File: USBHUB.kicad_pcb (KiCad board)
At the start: 4 copper layers, 214.6 x 214.6 mm, 214 parts, among them J1 USB_C_Receptacle, Q1 SI3421DV, Q2 SI3421DV, U1 CYPD3177_24x, U10 TPS20xxC, U11 USB_3_Type_A_Molex_484080003, U12 TPS20xxC, U13 USB_3_Type_A_Molex_484080003, U14 TPS20xxC, U15 USB_3_Type_A_Molex_484080003, U16 CYUSB3304-68LTXx, U2 TPS54331, U3 TLV75733PDBV, U4 TPS56637RPAR, U5 TVS2200DRVx, U6 PI3USB302-Ax, U7 TUSB522Px, U8 USB_3_Type_A_Molex_484080003, U9 TPS20xxC, Y1 26MHz

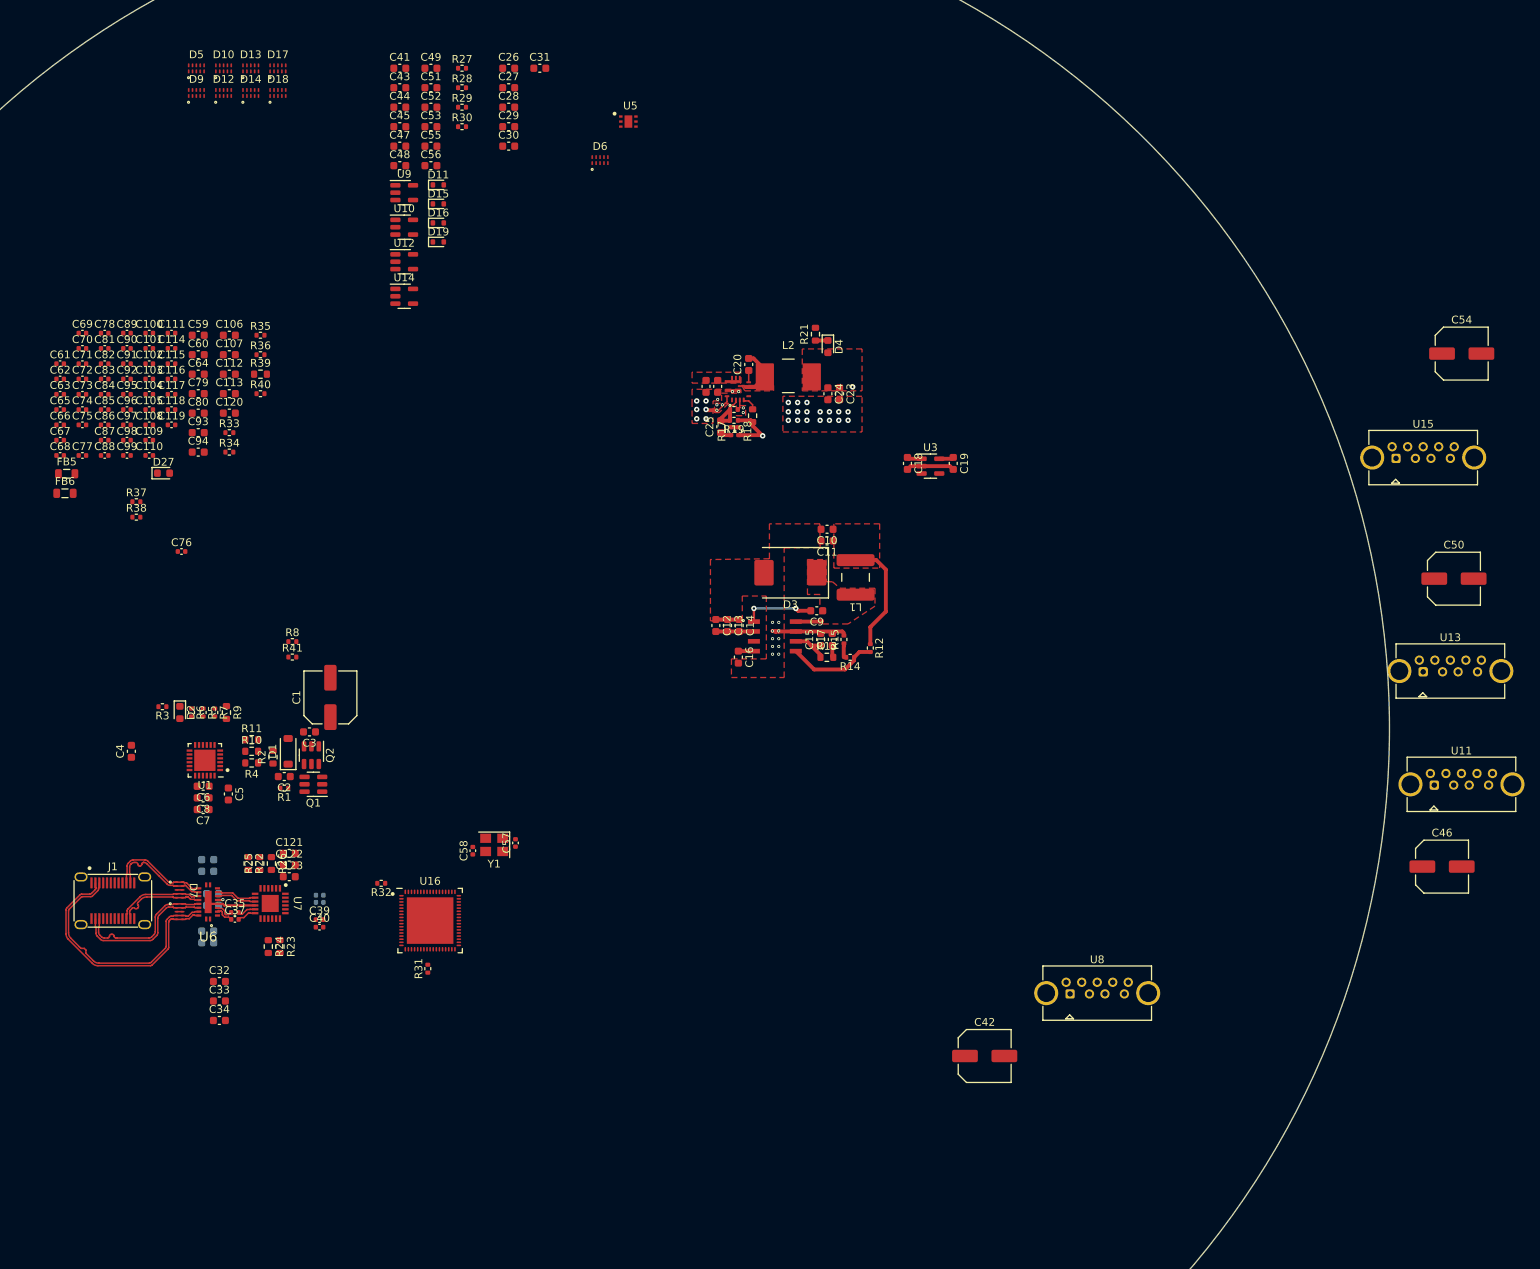
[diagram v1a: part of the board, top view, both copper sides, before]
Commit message: add RTL8153
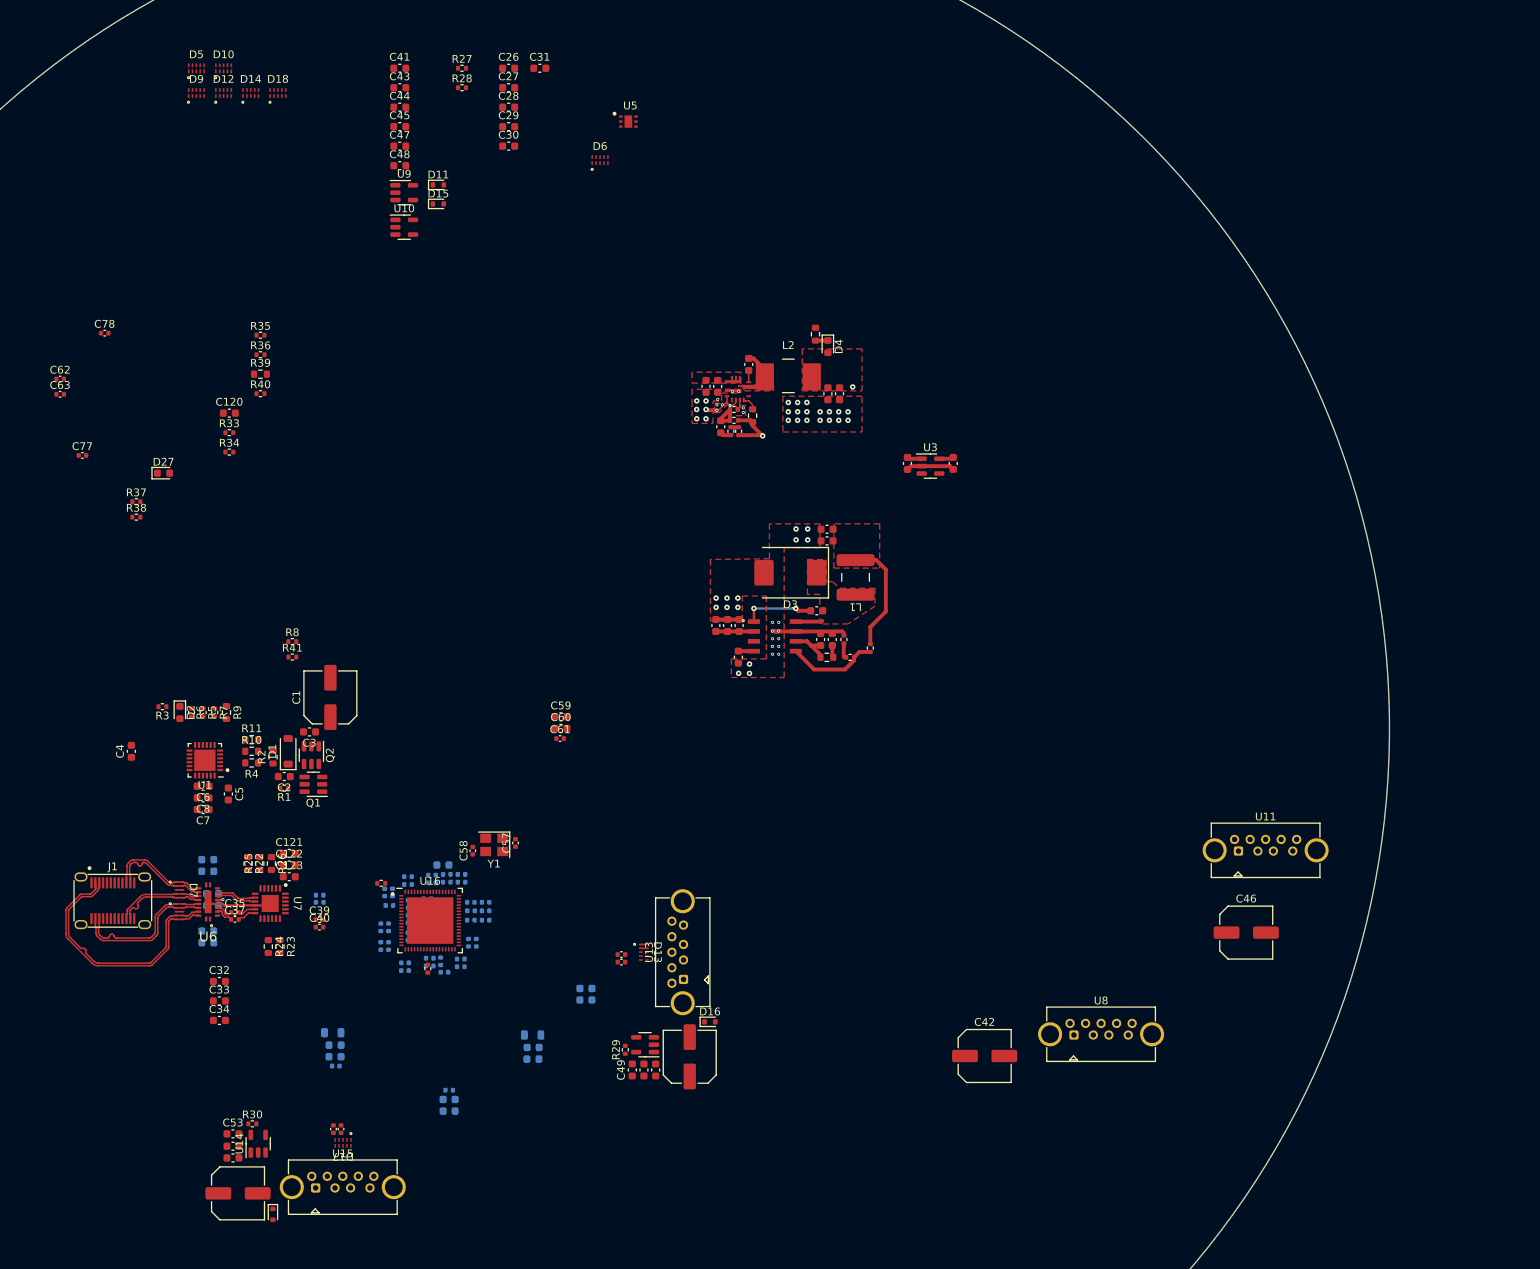
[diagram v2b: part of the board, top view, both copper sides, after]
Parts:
- C100, C101, C102, C103, C104, C105, C106, C107, C108, C109, C110, C111, C112, C113, C114, C115, C116, C117, C118, C119, C64, C65, C66, C67, C68, C69, C70, C71, C72, C73, C74, C75, C76, C79, C80, C81, C82, C83, C84, C85, C86, C87, C88, C93, C94, C95, C96, C97, C98, C99, FB5, FB6: moved to B.Cu
- moved C54 191.2 mm to (99.8, 175.7)
- moved U15 168.0 mm to (113.3, 174.9)
- moved D17 138.7 mm to (113.3, 169.2), turned to 180 degrees
- moved C53 132.3 mm to (99.2, 168.0)
- moved C49 131.6 mm to (150.6, 159.8), turned to 90 degrees
- moved C55 131.4 mm to (99.2, 169.6)
- moved R30 131.3 mm to (101.7, 166.7)
- moved C56 130.4 mm to (99.2, 171.1)
- moved C51 129.5 mm to (152.1, 159.8), turned to 90 degrees
- moved C52 127.4 mm to (153.6, 159.8), turned to 90 degrees
- moved D19 127.1 mm to (104.3, 178.4), turned to -90 degrees
- moved D13 124.6 mm to (152.1, 144.6), turned to -90 degrees
- moved R29 123.3 mm to (149.7, 157.2), turned to 90 degrees
- moved C50 116.1 mm to (158.0, 158.1), turned to 90 degrees
- moved U14 110.8 mm to (102.4, 169.3), turned to 90 degrees
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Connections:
- net HUB1_DS1_DM renamed HUB1_DS1_DN
- net HUB1_DS1_RXM renamed HUB1_DS1_RXN
- net HUB1_DS1_TXM renamed HUB1_DS1_TXN
- net HUB1_DS2_DM renamed HUB1_DS2_DN
- net HUB1_DS2_RXM renamed HUB1_DS2_RXN
- net HUB1_DS2_TXM renamed HUB1_DS2_TXN
- net HUB1_DS3_DM renamed HUB1_DS3_DN
- net HUB1_DS3_RXM renamed HUB1_DS3_RXN
- net HUB1_DS3_TXM renamed HUB1_DS3_TXN
- net HUB1_DS4_DM renamed HUB1_DS4_DN
- net HUB1_DS4_RXM renamed HUB1_DS4_RXN
- net HUB1_DS4_TXM renamed HUB1_DS4_TXN
- net Net-(U16-DS1_TXM) renamed /04 Hub Controller/HUB1_DS1_1_TXN
- net Net-(U16-DS1_TXP) renamed /04 Hub Controller/HUB1_DS1_1_TXP
- net Net-(U16-DS2_TXM) renamed /04 Hub Controller/HUB1_DS2_1_TXN
- net Net-(U16-DS2_TXP) renamed /04 Hub Controller/HUB1_DS2_1_TXP
- net Net-(U16-DS3_TXM) renamed /04 Hub Controller/HUB1_DS3_1_TXN
- net Net-(U16-DS3_TXP) renamed /04 Hub Controller/HUB1_DS3_1_TXP
- net Net-(U16-DS4_TXM) renamed /04 Hub Controller/HUB1_DS4_1_TXN
- net Net-(U16-DS4_TXP) renamed /04 Hub Controller/HUB1_DS4_1_TXP
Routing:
- net GND: track 31.7 -> 33.8 mm, vias 41 -> 54
- net HUB1_DS3_RXP: track 0.00 -> 0.78 mm
- net HUB1_DS3_RXN: track 0.00 -> 0.78 mm

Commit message: route power delivery controller
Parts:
- removed D18: PUSB3FR4Z, CakeUSB:PUSB3FR4Z
- removed D19: ESD5B5.0ST1G, Diode_SMD:D_SOD-523
- removed D27: RED, LED_SMD:LED_0603_1608Metric
- removed FB5, FB6: BLM21PG221SN1D, Inductor_SMD:L_0805_2012Metric
- removed U16: CYUSB3304-68LTXx, CakeUSB:CYUSB3304-68LTXx
- added C129: 100n, Capacitor_SMD:C_0402_1005Metric, F.Cu at (-59.6, 144.1)
- added C131: 4u7, Capacitor_SMD:C_0603_1608Metric, F.Cu at (-53.7, 125.5)
- added C132: 1u, Capacitor_SMD:C_0603_1608Metric, F.Cu at (-53.7, 128.0)
- added C133: 4u7, Capacitor_SMD:C_0603_1608Metric, F.Cu at (-53.7, 130.5)
- added C134: 4u7, Capacitor_SMD:C_0603_1608Metric, F.Cu at (-53.7, 133.0)
- added C135: 100n, Capacitor_SMD:C_0402_1005Metric, F.Cu at (-59.6, 146.1)
- added C136: 100n, Capacitor_SMD:C_0402_1005Metric, F.Cu at (-59.6, 148.0)
- added C137: 100n, Capacitor_SMD:C_0402_1005Metric, F.Cu at (-59.6, 150.0)
- added C138: 100n, Capacitor_SMD:C_0402_1005Metric, F.Cu at (-59.6, 152.0)
- added C139: 100n, Capacitor_SMD:C_0402_1005Metric, F.Cu at (-59.6, 153.9)
- added C140: 100n, Capacitor_SMD:C_0402_1005Metric, F.Cu at (-59.6, 155.9)
- added C141: 100n, Capacitor_SMD:C_0402_1005Metric, F.Cu at (-56.7, 144.1)
- added C142: 100n, Capacitor_SMD:C_0402_1005Metric, F.Cu at (-56.7, 146.1)
- added C143: 100n, Capacitor_SMD:C_0402_1005Metric, F.Cu at (-56.7, 148.0)
- added C144: 100n, Capacitor_SMD:C_0402_1005Metric, F.Cu at (-56.7, 150.0)
- added C145: 100n, Capacitor_SMD:C_0402_1005Metric, F.Cu at (-56.7, 152.0)
- added C146: 100n, Capacitor_SMD:C_0402_1005Metric, F.Cu at (-56.7, 153.9)
- added C147: 10n, Capacitor_SMD:C_0402_1005Metric, F.Cu at (-56.7, 155.6)
- added C148: 10n, Capacitor_SMD:C_0402_1005Metric, F.Cu at (-53.9, 144.1)
- added C149: 10n, Capacitor_SMD:C_0402_1005Metric, F.Cu at (-53.9, 146.1)
- added C150: 1n/2KV, Capacitor_SMD:C_0402_1005Metric, F.Cu at (83.6, 266.0)
- added C151: 10n, Capacitor_SMD:C_0402_1005Metric, F.Cu at (-53.9, 148.0)
- added C152: 10n, Capacitor_SMD:C_0402_1005Metric, F.Cu at (-53.9, 150.0)
- added FB1: BLM21PG221SN1D, Inductor_SMD:L_0805_2012Metric, F.Cu at (-60.2, 187.3)
- added FB2: BLM21PG221SN1D, Inductor_SMD:L_0805_2012Metric, F.Cu at (-60.2, 190.1)
- added J2: R-RJ45R08P-C000, CakeUSB:R-RJ45R08P-C000, F.Cu at (-72.5, 133.9)
- added R42: 2k49_1%, Resistor_SMD:R_0603_1608Metric, F.Cu at (-53.7, 135.6)
- added R43: 10k, Resistor_SMD:R_0402_1005Metric, F.Cu at (-51.0, 147.8)
- added R44: 75, Resistor_SMD:R_0603_1608Metric, F.Cu at (-53.7, 138.1)
- added R45: 75, Resistor_SMD:R_0603_1608Metric, F.Cu at (-49.7, 125.5)
- added R46: 75, Resistor_SMD:R_0603_1608Metric, F.Cu at (-49.7, 128.0)
- added R47: 75, Resistor_SMD:R_0603_1608Metric, F.Cu at (-49.7, 130.5)
- added R48: 1k, Resistor_SMD:R_0603_1608Metric, F.Cu at (-49.7, 133.0)
- added R49: 1k, Resistor_SMD:R_0603_1608Metric, F.Cu at (-49.7, 135.6)
- added T1: G24P02S, CakeUSB:G24P02S, F.Cu at (-72.5, 149.7)
- added Y2: 25MHz 18pF, Crystal:Crystal_SMD_2016-4Pin_2.0x1.6mm, F.Cu at (-50.5, 144.9)
- C100, C73: value 10n -> 1u; footprint Capacitor_SMD:C_0402_1005Metric -> Capacitor_SMD:C_0603_1608Metric; moved to F.Cu
- C101, C103, C70, C74, C76: value 1n -> 100n; moved to F.Cu
- C102, C104, C75, C83, C85: moved to F.Cu
- C105, C72, C99: value 1n -> 22u; footprint Capacitor_SMD:C_0402_1005Metric -> Capacitor_SMD:C_0603_1608Metric; moved to F.Cu
- C106: value 22u -> 1u; moved to F.Cu
- C107, C80: value 1u -> 100n; footprint Capacitor_SMD:C_0603_1608Metric -> Capacitor_SMD:C_0402_1005Metric; moved to F.Cu
- C108, C110, C66, C81, C95: value 100n -> 10n; moved to F.Cu
- C109, C111, C71, C82, C84, C88: value 10n -> 100n; moved to F.Cu
- C112, C79, C93: value 22u -> 10n; footprint Capacitor_SMD:C_0603_1608Metric -> Capacitor_SMD:C_0402_1005Metric; moved to F.Cu
- C113: value 1u -> 22u; moved to F.Cu
- C114, C116, C118, C36: footprint Capacitor_SMD:C_0402_1005Metric -> Capacitor_SMD:C_0603_1608Metric; moved to F.Cu
- C115, C119: value 10n -> 150u; footprint Capacitor_SMD:C_0402_1005Metric -> Capacitor_SMD:C_Elec_6.3x7.7; moved to F.Cu
- C117: value 10n -> 100n; footprint Capacitor_SMD:C_0402_1005Metric -> Capacitor_SMD:C_0603_1608Metric; moved to F.Cu
- C120: value 22u -> 100n
- C121, C124: value 10u -> 100n
- C123: value 100n -> 150u; footprint Capacitor_SMD:C_0603_1608Metric -> Capacitor_SMD:C_Elec_6.3x7.7
- C126: value 100n -> 27p; footprint Capacitor_SMD:C_0603_1608Metric -> Capacitor_SMD:C_0402_1005Metric; moved to F.Cu
- C127: value 10u -> 27p; footprint Capacitor_SMD:C_0603_1608Metric -> Capacitor_SMD:C_0402_1005Metric; moved to F.Cu
- C128: value 100n -> 10u
- C130: value 10u -> 1u
- C26, C27, C28, C29, C44, C45, C47, C48, C49, C55, C56: footprint Capacitor_SMD:C_0603_1608Metric -> Capacitor_SMD:C_0402_1005Metric
- C35, C38: value 100n -> 10u; footprint Capacitor_SMD:C_0402_1005Metric -> Capacitor_SMD:C_0603_1608Metric
- C37: footprint Capacitor_SMD:C_0402_1005Metric -> Capacitor_SMD:C_0603_1608Metric
- C39, C40: value 100n -> 10u; footprint Capacitor_SMD:C_0402_1005Metric -> Capacitor_SMD:C_0603_1608Metric; moved to B.Cu
- C41, C43, D7: moved to B.Cu
- C42: value 150u -> 100n; footprint Capacitor_SMD:C_Elec_6.3x7.7 -> Capacitor_SMD:C_0603_1608Metric; moved to B.Cu
- C46, C54: value 150u -> 100n; footprint Capacitor_SMD:C_Elec_6.3x7.7 -> Capacitor_SMD:C_0402_1005Metric
- C50: value 150u -> 10p; footprint Capacitor_SMD:C_Elec_6.3x7.7 -> Capacitor_SMD:C_0402_1005Metric
- C51: value 100n -> 10p; footprint Capacitor_SMD:C_0603_1608Metric -> Capacitor_SMD:C_0402_1005Metric
- C52: value 100n -> 22u
- C53: value 100n -> 1u
- C57: value 10p -> 1u; footprint Capacitor_SMD:C_0402_1005Metric -> Capacitor_SMD:C_0603_1608Metric
- C58: value 10p -> 10n
- C59: value 22u -> 100n; footprint Capacitor_SMD:C_0603_1608Metric -> Capacitor_SMD:C_0402_1005Metric
- C60: value 1u -> 10n; footprint Capacitor_SMD:C_0603_1608Metric -> Capacitor_SMD:C_0402_1005Metric
- C61, C63, C90, C92: value 100n -> 1n
- C62, C77, C89, C91: value 100n -> 10n
- C64: value 1u -> 10n; footprint Capacitor_SMD:C_0603_1608Metric -> Capacitor_SMD:C_0402_1005Metric; moved to F.Cu
- C65, C67, C69, C96, C98: value 10n -> 1n; moved to F.Cu
- C68, C97: value 1n -> 10n; moved to F.Cu
- C86: value 10n -> 22u; footprint Capacitor_SMD:C_0402_1005Metric -> Capacitor_SMD:C_0603_1608Metric; moved to F.Cu
- C87: value 100n -> 1u; footprint Capacitor_SMD:C_0402_1005Metric -> Capacitor_SMD:C_0603_1608Metric; moved to F.Cu
- C94: value 1u -> 1n; footprint Capacitor_SMD:C_0603_1608Metric -> Capacitor_SMD:C_0402_1005Metric; moved to F.Cu
- D11: value ESD5B5.0ST1G -> PUSB3FR4Z; footprint Diode_SMD:D_SOD-523 -> CakeUSB:PUSB3FR4Z
- D14: value PUSB3FR4Z -> RED; footprint CakeUSB:PUSB3FR4Z -> LED_SMD:LED_0603_1608Metric
- D17: value PUSB3FR4Z -> ESD5B5.0ST1G; footprint CakeUSB:PUSB3FR4Z -> Diode_SMD:D_SOD-523
- R1: footprint Resistor_SMD:R_0402_1005Metric -> Resistor_SMD:R_0603_1608Metric
- R12: value 10k -> 5k1; footprint Resistor_SMD:R_0402_1005Metric -> Resistor_SMD:R_0603_1608Metric
- R13: value 953 -> 10k; footprint Resistor_SMD:R_0603_1608Metric -> Resistor_SMD:R_0402_1005Metric
- R14: value 10k -> 953; footprint Resistor_SMD:R_0402_1005Metric -> Resistor_SMD:R_0603_1608Metric
- R16: value 100k -> 10k; footprint Resistor_SMD:R_0603_1608Metric -> Resistor_SMD:R_0402_1005Metric
- R17: value 10k -> 100k; footprint Resistor_SMD:R_0402_1005Metric -> Resistor_SMD:R_0603_1608Metric
- R19: value 73k2 -> 10k
- R20: value 10k -> 73k2
- R21, R39: value 5k1 -> 10k; footprint Resistor_SMD:R_0603_1608Metric -> Resistor_SMD:R_0402_1005Metric
- R23: value 1k -> 5k1
- R27: value 10k -> 1k; footprint Resistor_SMD:R_0402_1005Metric -> Resistor_SMD:R_0603_1608Metric
- R28: value 10k -> 200_1%
- R29: value 10k -> 6k04_1%
- R31: value 200_1% -> 10k
- R32: value 6k04_1% -> 10k
- R35, R36: value 10k -> 2k
- R37: value 2k -> 5k1; footprint Resistor_SMD:R_0402_1005Metric -> Resistor_SMD:R_0603_1608Metric
- R38, R41: value 2k -> 10k
- R9: value 5k1 -> 2k; footprint Resistor_SMD:R_0603_1608Metric -> Resistor_SMD:R_0402_1005Metric
- U10, U9: value TPS20xxC -> USB_3_Type_A_Molex_484080003; footprint Package_TO_SOT_SMD:SOT-23-5 -> CakeUSB:Molex_484080003
- U11: value USB_3_Type_A_Molex_484080003 -> CYUSB3304-68LTXx; footprint CakeUSB:Molex_484080003 -> CakeUSB:CYUSB3304-68LTXx
- U13: value USB_3_Type_A_Molex_484080003 -> TPS20xxC; footprint CakeUSB:Molex_484080003 -> Package_TO_SOT_SMD:SOT-23-5
- U15: value USB_3_Type_A_Molex_484080003 -> RTL8153-VB-CG; footprint CakeUSB:Molex_484080003 -> CakeUSB:RTL8153B-VB-CG
- moved C31 317.3 mm to (-91.8, 248.8)
- moved C30 305.8 mm to (-91.8, 246.3)
- moved C47 284.3 mm to (-80.3, 241.9)
- moved C44 283.7 mm to (-80.3, 235.9)
- moved C45 283.3 mm to (-80.3, 237.9)
- moved D11 275.1 mm to (-70.9, 238.3)
- moved D15 273.9 mm to (-82.0, 226.8)
- moved D12 267.5 mm to (-70.9, 241.4)
- moved R28 266.0 mm to (-67.2, 213.3)
- moved D10 265.1 mm to (-70.9, 235.1)
- moved U9 261.5 mm to (-60.6, 234.7)
- moved D9 258.0 mm to (-70.9, 231.9)
- moved D14 254.3 mm to (-63.7, 227.3)
- moved D16 254.2 mm to (-82.0, 229.3)
- moved U13 249.7 mm to (-81.3, 218.9), turned to 0 degrees
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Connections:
- C100 pad 1: +1V2 -> Net-(C100-Pad1)
- C101 pad 1: +1V2 -> Net-(C100-Pad1)
- C102 pad 1: +1V2 -> Net-(C100-Pad1)
- C103 pad 1: +1V2 -> +3V3
- C104 pad 1: +1V2 -> +3V3
- C105 pad 1: +1V2 -> +3V3
- C106 pad 1: Net-(C106-Pad1) -> +3V3
- C107 pad 1: Net-(C106-Pad1) -> +3V3
- C108 pad 1: Net-(C106-Pad1) -> +3V3
- C109 pad 1: Net-(C106-Pad1) -> +3V3
- C113 pad 1: +3V3 -> /04 Hub Controller/RESETN
- C114 pad 1: +3V3 -> GND
- C114 pad 2: GND -> +5V
- C115 pad 1: +3V3 -> GND
- C115 pad 2: GND -> /03 USB_DFP/USB_DS1_VBUS
- C116 pad 1: +3V3 -> GND
- C116 pad 2: GND -> /03 USB_DFP/USB_DS1_VBUS
- C117 pad 1: +3V3 -> GND
- C117 pad 2: GND -> /03 USB_DFP/USB_DS1_VBUS
- C118 pad 1: +3V3 -> GND
- C118 pad 2: GND -> +5V
- C119 pad 1: +3V3 -> GND
- C119 pad 2: GND -> /03 USB_DFP/USB_DS2_VBUS
- C120 pad 1: /04 Hub Controller/RESETN -> GND
- C120 pad 2: GND -> /03 USB_DFP/USB_DS2_VBUS
- C121 pad 1: +3V3 -> GND
- C121 pad 2: GND -> /03 USB_DFP/USB_DS2_VBUS
- C122 pad 1: +3V3 -> GND
- C122 pad 2: GND -> +5V
- C123 pad 1: +3V3 -> GND
- C123 pad 2: GND -> /03 USB_DFP/USB_DS3_VBUS
- C124 pad 1: +3V3 -> GND
- C124 pad 2: GND -> /03 USB_DFP/USB_DS3_VBUS
- C125 pad 1: +3V3 -> GND
- C125 pad 2: GND -> /03 USB_DFP/USB_DS3_VBUS
- C126 pad 1: +3V3 -> Net-(U15A-CKXTAL1)
- C127 pad 1: +3V3 -> Net-(U15A-CKXTAL2)
- C128 pad 1: +3V3 -> GND
- C128 pad 2: GND -> +5V
- C130 pad 1: +3V3 -> Net-(U15B-DVDD10_UPS_REGOUT)
- C35 pad 1: /02 USB UFP/UFP_TX- -> +3V3
- C35 pad 2: /02 USB UFP/UFP_TX_A_N -> GND
- C36 pad 1: /02 USB UFP/UFP_RX_B_N -> +3V3
- C36 pad 2: USB_UFP_RXN -> GND
- C37 pad 1: /02 USB UFP/UFP_TX+ -> +3V3
- C37 pad 2: /02 USB UFP/UFP_TX_A_P -> GND
- C38 pad 1: /02 USB UFP/UFP_RX_B_P -> +3V3
- C38 pad 2: USB_UFP_RXP -> GND
- C39 pad 1: /02 USB UFP/UFP_TX_B_N -> +3V3
- C39 pad 2: USB_UFP_TXN -> GND
- C40 pad 1: /02 USB UFP/UFP_TX_B_P -> +3V3
- C40 pad 2: USB_UFP_TXP -> GND
- C41 pad 1: GND -> +3V3
- C41 pad 2: +5V -> GND
- C42 pad 1: GND -> +3V3
- C42 pad 2: /03 USB_DFP/USB_DS1_VBUS -> GND
- C43 pad 1: GND -> +3V3
- C43 pad 2: /03 USB_DFP/USB_DS1_VBUS -> GND
- C44 pad 1: GND -> /02 USB UFP/UFP_RX_B_N
- C44 pad 2: /03 USB_DFP/USB_DS1_VBUS -> USB_UFP_RXN
- C45 pad 1: GND -> /02 USB UFP/UFP_RX_B_P
- C45 pad 2: +5V -> USB_UFP_RXP
- C46 pad 1: GND -> /02 USB UFP/UFP_TX-
- C46 pad 2: /03 USB_DFP/USB_DS2_VBUS -> /02 USB UFP/UFP_TX_A_N
- C47 pad 1: GND -> /02 USB UFP/UFP_TX_B_N
- C47 pad 2: /03 USB_DFP/USB_DS2_VBUS -> USB_UFP_TXN
- C48 pad 1: GND -> /02 USB UFP/UFP_TX+
- C48 pad 2: /03 USB_DFP/USB_DS2_VBUS -> /02 USB UFP/UFP_TX_A_P
- C49 pad 1: GND -> /02 USB UFP/UFP_TX_B_P
- C49 pad 2: +5V -> USB_UFP_TXP
- C50 pad 1: GND -> Net-(U11-XTL_OUT)
- C50 pad 2: /03 USB_DFP/USB_DS3_VBUS -> GND
- C51 pad 1: GND -> Net-(U11-XTL_IN)
- C51 pad 2: /03 USB_DFP/USB_DS3_VBUS -> GND
- C52 pad 1: GND -> +1V2
- C52 pad 2: /03 USB_DFP/USB_DS3_VBUS -> GND
- C53 pad 1: GND -> +1V2
- C53 pad 2: +5V -> GND
- C54 pad 1: GND -> +1V2
- C54 pad 2: /03 USB_DFP/USB_DS4_VBUS -> GND
- C55 pad 1: GND -> /04 Hub Controller/HUB1_DS1_1_TXP
- C55 pad 2: /03 USB_DFP/USB_DS4_VBUS -> HUB1_DS1_TXP
- C56 pad 1: GND -> /04 Hub Controller/HUB1_DS1_1_TXN
- C56 pad 2: /03 USB_DFP/USB_DS4_VBUS -> HUB1_DS1_TXN
- C57 pad 1: Net-(U16-XTL_OUT) -> +1V2
- C58 pad 1: Net-(U16-XTL_IN) -> +1V2
- C62 pad 1: /04 Hub Controller/HUB1_DS1_1_TXP -> +1V2
- C62 pad 2: HUB1_DS1_TXP -> GND
- C63 pad 1: /04 Hub Controller/HUB1_DS1_1_TXN -> +1V2
- C63 pad 2: HUB1_DS1_TXN -> GND
- C70 pad 1: +1V2 -> /04 Hub Controller/HUB1_DS2_1_TXP
- C70 pad 2: GND -> HUB1_DS2_TXP
- C71 pad 1: +1V2 -> /04 Hub Controller/HUB1_DS2_1_TXN
- C71 pad 2: GND -> HUB1_DS2_TXN
- C72 pad 1: +1V2 -> /04 Hub Controller/DVDD12
- C73 pad 1: +1V2 -> /04 Hub Controller/DVDD12
- C74 pad 1: +1V2 -> /04 Hub Controller/DVDD12
- C75 pad 1: +1V2 -> /04 Hub Controller/DVDD12
- C76 pad 1: +1V2 -> /04 Hub Controller/DVDD12
- C77 pad 1: /04 Hub Controller/HUB1_DS2_1_TXP -> /04 Hub Controller/DVDD12
- C77 pad 2: HUB1_DS2_TXP -> GND
- C78 pad 1: /04 Hub Controller/HUB1_DS2_1_TXN -> /04 Hub Controller/DVDD12
- C78 pad 2: HUB1_DS2_TXN -> GND
- C82 pad 1: /04 Hub Controller/DVDD12 -> /04 Hub Controller/HUB1_DS3_1_TXP
- C82 pad 2: GND -> HUB1_DS3_TXP
- C83 pad 1: /04 Hub Controller/DVDD12 -> /04 Hub Controller/HUB1_DS3_1_TXN
- C83 pad 2: GND -> HUB1_DS3_TXN
- C84 pad 1: /04 Hub Controller/DVDD12 -> /04 Hub Controller/HUB1_DS4_1_TXP
- C84 pad 2: GND -> HUB1_DS4_TXP
- C85 pad 1: /04 Hub Controller/DVDD12 -> /04 Hub Controller/HUB1_DS4_1_TXN
- C85 pad 2: GND -> HUB1_DS4_TXN
- C86 pad 1: /04 Hub Controller/DVDD12 -> +1V2
- C87 pad 1: /04 Hub Controller/DVDD12 -> +1V2
- C88 pad 1: /04 Hub Controller/DVDD12 -> +1V2
- C89 pad 1: /04 Hub Controller/HUB1_DS3_1_TXP -> +1V2
- C89 pad 2: HUB1_DS3_TXP -> GND
- C90 pad 1: /04 Hub Controller/HUB1_DS3_1_TXN -> +1V2
- C90 pad 2: HUB1_DS3_TXN -> GND
- C91 pad 1: /04 Hub Controller/HUB1_DS4_1_TXP -> +1V2
- C91 pad 2: HUB1_DS4_TXP -> GND
- C92 pad 1: /04 Hub Controller/HUB1_DS4_1_TXN -> +1V2
- C92 pad 2: HUB1_DS4_TXN -> GND
- C99 pad 1: +1V2 -> Net-(C100-Pad1)
- D10 pad 1: HUB1_DS2_RXN -> HUB1_DS3_RXN
- D10 pad 2: HUB1_DS2_RXP -> HUB1_DS3_RXP
- D10 pad 4: HUB1_DS2_TXN -> HUB1_DS3_TXN
- D10 pad 5: HUB1_DS2_TXP -> HUB1_DS3_TXP
- D11 pad 1: /03 USB_DFP/USB_DS1_VBUS -> unconnected-(D11-CH1-Pad1)
- D11 pad 2: GND -> unconnected-(D11-CH2-Pad2)
- D12 pad 1: unconnected-(D12-CH1-Pad1) -> HUB1_DS2_RXN
- D12 pad 2: unconnected-(D12-CH2-Pad2) -> HUB1_DS2_RXP
- D12 pad 4: HUB1_DS2_DN -> HUB1_DS2_TXN
- D12 pad 5: HUB1_DS2_DP -> HUB1_DS2_TXP
- D13 pad 1: HUB1_DS3_RXN -> unconnected-(D13-CH1-Pad1)
- D13 pad 2: HUB1_DS3_RXP -> unconnected-(D13-CH2-Pad2)
- D13 pad 4: HUB1_DS3_TXN -> HUB1_DS2_DN
- D13 pad 5: HUB1_DS3_TXP -> HUB1_DS2_DP
- D14 pad 1: unconnected-(D14-CH1-Pad1) -> Net-(D14-K)
- D14 pad 2: unconnected-(D14-CH2-Pad2) -> /04 Hub Controller/SUSPEND
- D15 pad 1: /03 USB_DFP/USB_DS2_VBUS -> /03 USB_DFP/USB_DS1_VBUS
- D16 pad 1: /03 USB_DFP/USB_DS3_VBUS -> /03 USB_DFP/USB_DS2_VBUS
- D17 pad 1: HUB1_DS4_RXN -> /03 USB_DFP/USB_DS3_VBUS
- D17 pad 2: HUB1_DS4_RXP -> GND
- D5 pad 1: HUB1_DS1_RXN -> /02 USB UFP/UFP_RX2-
- D5 pad 2: HUB1_DS1_RXP -> /02 USB UFP/UFP_RX2+
- D5 pad 4: HUB1_DS1_TXN -> /02 USB UFP/UFP_TX2-
- D5 pad 5: HUB1_DS1_TXP -> /02 USB UFP/UFP_TX2+
- D6 pad 1: USB_UFP_DM -> /02 USB UFP/UFP_RX1-
- D6 pad 2: USB_UFP_DP -> /02 USB UFP/UFP_RX1+
- D6 pad 4: USB_UFP_CC1 -> /02 USB UFP/UFP_TX1-
- D6 pad 5: USB_UFP_CC2 -> /02 USB UFP/UFP_TX1+
- D7 pad 1: /02 USB UFP/UFP_RX2- -> USB_UFP_DP
- D7 pad 2: /02 USB UFP/UFP_RX2+ -> USB_UFP_DN
- D7 pad 4: /02 USB UFP/UFP_TX2- -> USB_UFP_CC2
- D7 pad 5: /02 USB UFP/UFP_TX2+ -> USB_UFP_CC1
- D8 pad 1: /02 USB UFP/UFP_RX1- -> HUB1_DS1_RXN
- D8 pad 2: /02 USB UFP/UFP_RX1+ -> HUB1_DS1_RXP
- D8 pad 4: /02 USB UFP/UFP_TX1- -> HUB1_DS1_TXN
- D8 pad 5: /02 USB UFP/UFP_TX1+ -> HUB1_DS1_TXP
- J1 pad A7: USB_UFP_DM -> USB_UFP_DN
- J1 pad B7: USB_UFP_DM -> USB_UFP_DN
- R10 pad 1: Net-(U1-ISNK_COARSE) -> /01 Power/USB_PD_VDDD_3V3
- R10 pad 2: GND -> Net-(U1-ISNK_COARSE)
- R11 pad 1: Net-(U1-ISNK_FINE) -> Net-(U1-ISNK_COARSE)
- R12 pad 1: +1V2 -> Net-(U1-ISNK_FINE)
- R12 pad 2: Net-(U2-VSENSE) -> GND
- R13 pad 1: Net-(U2-COMP) -> +1V2
- R13 pad 2: Net-(C17-Pad1) -> Net-(U2-VSENSE)
- R14 pad 1: Net-(U2-VSENSE) -> Net-(U2-COMP)
- R14 pad 2: Net-(R14-Pad2) -> Net-(C17-Pad1)
- R15 pad 1: Net-(R14-Pad2) -> Net-(U2-VSENSE)
- R15 pad 2: GND -> Net-(R15-Pad2)
- R16 pad 1: Net-(U4-PG) -> Net-(R15-Pad2)
- R16 pad 2: +5V -> GND
- R17 pad 1: Net-(C25-Pad1) -> Net-(U4-PG)
- R17 pad 2: Net-(R17-Pad2) -> +5V
- R18 pad 1: Net-(R17-Pad2) -> Net-(C25-Pad1)
- R18 pad 2: +5V -> Net-(R18-Pad2)
- R19 pad 1: +5V -> Net-(R18-Pad2)
- R19 pad 2: Net-(U4-FB) -> +5V
- R20 pad 1: Net-(U4-FB) -> +5V
- R20 pad 2: GND -> Net-(U4-FB)
- R21 pad 1: Net-(D4-K) -> Net-(U4-FB)
- R22 pad 1: +3V3 -> Net-(D4-K)
- R22 pad 2: Net-(U7-EN_RXD) -> GND
- R23 pad 1: Net-(U7-EQ2) -> +3V3
- R23 pad 2: +3V3 -> Net-(U7-EN_RXD)
- R24 pad 1: Net-(U7-OS1) -> +3V3
- R24 pad 2: GND -> Net-(U7-EQ1)
- R25 pad 1: Net-(U7-OS2) -> Net-(U7-EQ2)
- R25 pad 2: GND -> +3V3
- R26 pad 1: +3V3 -> Net-(U7-OS1)
- R26 pad 2: Net-(U7-EQ1) -> GND
- R27 pad 1: +5V -> Net-(U7-OS2)
- R27 pad 2: Net-(U9-~{FLT}) -> GND
- R28 pad 1: +5V -> GND
- R28 pad 2: Net-(U10-~{FLT}) -> Net-(U11-RREF_SS)
- R29 pad 1: +5V -> Net-(U11-RREF_USB2)
- R29 pad 2: Net-(U12-~{FLT}) -> GND
- R30 pad 1: +5V -> +3V3
- R30 pad 2: Net-(U14-~{FLT}) -> Net-(U11-MODE_SEL[1])
- R31 pad 1: GND -> Net-(U11-RESERVED2)
- R31 pad 2: Net-(U16-RREF_SS) -> +3V3
- R32 pad 1: Net-(U16-RREF_USB2) -> +3V3
- R32 pad 2: GND -> Net-(U11-MODE_SEL[0])
- R33 pad 1: +3V3 -> Net-(U11-RESERVED1)
- R33 pad 2: Net-(U16-MODE_SEL[1]) -> +3V3
- R34 pad 1: Net-(U16-RESERVED2) -> +3V3
- R34 pad 2: +3V3 -> /04 Hub Controller/RESETN
- R35 pad 2: Net-(U16-MODE_SEL[0]) -> /04 Hub Controller/I2C_DATA
- R36 pad 1: Net-(U16-RESERVED1) -> +3V3
- R36 pad 2: +3V3 -> /04 Hub Controller/I2C_CLK
- R37 pad 1: +3V3 -> Net-(D14-K)
- R37 pad 2: /04 Hub Controller/I2C_DATA -> GND
- R38 pad 1: +3V3 -> +5V
- R38 pad 2: /04 Hub Controller/I2C_CLK -> Net-(U12-~{FLT})
- R39 pad 1: Net-(D27-K) -> +5V
- R39 pad 2: GND -> Net-(U13-~{FLT})
- R40 pad 1: +3V3 -> +5V
- R40 pad 2: /04 Hub Controller/RESETN -> Net-(U14-~{FLT})
- R41 pad 1: /01 Power/USB_PD_VDDD_3V3 -> GND
- R41 pad 2: Net-(R41-Pad2) -> Net-(U15A-EEDI/SPISDI/ENSWREG)
- R8 pad 1: Net-(R41-Pad2) -> /01 Power/USB_PD_VDDD_3V3
- R8 pad 2: USB_UFP_FLIP -> Net-(R8-Pad2)
- R9 pad 1: /01 Power/USB_PD_VDDD_3V3 -> Net-(R8-Pad2)
- R9 pad 2: Net-(U1-ISNK_COARSE) -> USB_UFP_FLIP
- U10 pad 2: GND -> HUB1_DS2_DN
- U10 pad 3: Net-(U10-~{FLT}) -> HUB1_DS2_DP
- U10 pad 4: HUB1_PWR_EN_DS -> GND
- U10 pad 5: +5V -> HUB1_DS2_RXN
- U11 pad 1: /03 USB_DFP/USB_DS2_VBUS -> /04 Hub Controller/DVDD12
- U11 pad 10: unconnected-(U11-SHIELD-Pad10) -> +1V2
- U11 pad 2: HUB1_DS2_DN -> Net-(U11-RREF_USB2)
- U11 pad 3: HUB1_DS2_DP -> /04 Hub Controller/DVDD12
- U11 pad 4: GND -> Net-(C100-Pad1)
- U11 pad 5: HUB1_DS2_RXN -> USB_UFP_TXN
- U11 pad 6: HUB1_DS2_RXP -> USB_UFP_TXP
- U11 pad 7: GND -> +1V2
- U11 pad 8: HUB1_DS2_TXN -> USB_UFP_RXN
- U11 pad 9: HUB1_DS2_TXP -> USB_UFP_RXP
- U12 pad 1: /03 USB_DFP/USB_DS3_VBUS -> /03 USB_DFP/USB_DS1_VBUS
- U13 pad 1: /03 USB_DFP/USB_DS3_VBUS -> /03 USB_DFP/USB_DS2_VBUS
- U13 pad 2: HUB1_DS3_DN -> GND
- U13 pad 3: HUB1_DS3_DP -> Net-(U13-~{FLT})
- U13 pad 4: GND -> HUB1_PWR_EN_DS
- U13 pad 5: HUB1_DS3_RXN -> +5V
- U14 pad 1: /03 USB_DFP/USB_DS4_VBUS -> /03 USB_DFP/USB_DS3_VBUS
- U15 pad 1: /03 USB_DFP/USB_DS4_VBUS -> Net-(T1-X1+)
- U15 pad 10: unconnected-(U15-SHIELD-Pad10) -> Net-(T1-X4-)
- U15 pad 2: HUB1_DS4_DN -> Net-(T1-X1-)
- U15 pad 3: HUB1_DS4_DP -> /05 Ethernet USB IC/VDD10
- U15 pad 4: GND -> Net-(T1-X2+)
- U15 pad 5: HUB1_DS4_RXN -> Net-(T1-X2-)
- U15 pad 6: HUB1_DS4_RXP -> Net-(T1-X3+)
- U15 pad 7: GND -> Net-(T1-X3-)
- U15 pad 8: HUB1_DS4_TXN -> /05 Ethernet USB IC/VDD10
- U15 pad 9: HUB1_DS4_TXP -> Net-(T1-X4+)
- U9 pad 1: /03 USB_DFP/USB_DS1_VBUS -> /03 USB_DFP/USB_DS3_VBUS
- U9 pad 2: GND -> HUB1_DS3_DN
- U9 pad 3: Net-(U9-~{FLT}) -> HUB1_DS3_DP
- U9 pad 4: HUB1_PWR_EN_DS -> GND
- U9 pad 5: +5V -> HUB1_DS3_RXN
- Y1 pad 1: Net-(U16-XTL_OUT) -> Net-(U11-XTL_OUT)
- Y1 pad 3: Net-(U16-XTL_IN) -> Net-(U11-XTL_IN)
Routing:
- net GND: track 33.8 -> 85.4 mm, vias 54 -> 87
- net /01 Power/USB_PD_VDDD_3V3: track 0.00 -> 25.5 mm, vias 0 -> 3
- net +20V: track 0.00 -> 17.6 mm, vias 0 -> 11
- net Net-(D1-A): track 0.00 -> 15.5 mm, vias 0 -> 3
- net VBUS: track 0.00 -> 8.44 mm, vias 0 -> 10
- net USB_UFP_DN: track 0.00 -> 7.84 mm, vias 0 -> 2
- net USB_UFP_DP: track 0.00 -> 7.75 mm, vias 0 -> 2
- net /01 Power/FAULT: track 0.00 -> 6.51 mm, vias 0 -> 2
- net Net-(U1-ISNK_COARSE): track 0.00 -> 6.39 mm, vias 0 -> 2
- net Net-(D1-K): track 0.00 -> 5.89 mm
- net USB_UFP_FLIP: track 0.00 -> 5.46 mm, vias 0 -> 2
- net Net-(U1-HPI_SCL): track 0.00 -> 3.69 mm
- net +3V3: track 2.59 -> 6.26 mm, vias 1 -> 2
- net Net-(U1-VBUS_FET_EN): track 0.00 -> 2.73 mm
- net Net-(U1-ISNK_FINE): track 0.00 -> 2.64 mm
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- added copper zone on In2.Cu, net +20V
- added copper zone on F.Cu, net Net-(D1-A)
- added copper zone on F.Cu, net VBUS
- added copper zone on In2.Cu, net VBUS

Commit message: settle on a layout
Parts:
- added H1: MountingHole, MountingHole:MountingHole_2.7mm_M2.5, F.Cu at (73.2, 60.1)
- added H2: MountingHole, MountingHole:MountingHole_2.7mm_M2.5, F.Cu at (73.2, 67.0)
- added H3: MountingHole, MountingHole:MountingHole_2.7mm_M2.5, F.Cu at (73.2, 74.0)
- added H4: MountingHole, MountingHole:MountingHole_2.7mm_M2.5, F.Cu at (73.2, 81.0)
- added J3: Screw_Terminal_01x02, CakeUSB:TerminalBlock_WJ103-5.0-2P, F.Cu at (102.4, 99.7)
- C10, C100, C101, C102, C103, C104, C105, C106, C107, C108, C109, C11, C110, C111, C112, C113, C12, C13, C133, C134, C135, C136, C137, C139, C14, C140, C141, C142, C143, C144, C145, C146, C147, C148, C149, C15, C150, C151, C152, C16, C17, C18, C19, C26, C27, C28, C29, C35, C44, C45, C52, C53, C54, C57, C58, C59, C60, C61, C62, C63, C64, C65, C66, C67, C68, C69, C72, C73, C74, C75, C76, C77, C78, C79, C80, C81, C86, C87, C88, C89, C9, C90, C91, C92, C93, C94, C95, C96, C97, C98, C99, D3, FB1, FB2, L1, R13, R14, R15, R16, R34, R44, R45, R46, R47, R48, R49, U2, U3: moved to B.Cu
- C124, C125, C128: moved to F.Cu
- C30, C31, C33, C34, C41, C42, C43: footprint Capacitor_SMD:C_0603_1608Metric -> Capacitor_SMD:C_0402_1005Metric
- C36, C37: footprint Capacitor_SMD:C_0603_1608Metric -> Capacitor_SMD:C_0402_1005Metric; moved to B.Cu
- moved D15 262.0 mm to (156.9, 119.2)
- moved C115 260.4 mm to (150.9, 114.7)
- moved R38 260.1 mm to (151.8, 106.3)
- moved U12 256.5 mm to (152.5, 108.8), turned to 90 degrees
- moved C119 249.2 mm to (151.5, 158.7), turned to 90 degrees
- moved D16 249.1 mm to (154.8, 152.0)
- moved D9 240.2 mm to (142.6, 121.8), turned to 90 degrees
- moved D13 237.8 mm to (143.2, 141.1), turned to 90 degrees
- moved U13 235.4 mm to (145.8, 156.9), turned to 180 degrees
- moved D12 234.4 mm to (143.1, 145.8), turned to -90 degrees
- moved R39 233.0 mm to (143.2, 157.7), turned to 90 degrees
- moved C120 230.1 mm to (147.2, 160.2), turned to 90 degrees
- moved C121 229.3 mm to (145.7, 160.2), turned to 90 degrees
- moved R40 228.5 mm to (141.0, 168.2), turned to -90 degrees
- moved U14 226.3 mm to (138.4, 169.1)
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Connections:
- net Net-(T1-D1+) renamed /05 Ethernet USB IC/ETH1+
- net Net-(T1-D1-) renamed /05 Ethernet USB IC/ETH1-
- net Net-(T1-D2+) renamed /05 Ethernet USB IC/ETH2+
- net Net-(T1-D2-) renamed /05 Ethernet USB IC/ETH2-
- net Net-(T1-D3+) renamed /05 Ethernet USB IC/ETH3+
- net Net-(T1-D3-) renamed /05 Ethernet USB IC/ETH3-
- net Net-(T1-D4+) renamed /05 Ethernet USB IC/ETH4+
- net Net-(T1-D4-) renamed /05 Ethernet USB IC/ETH4-
- net Net-(T1-X1+) renamed /05 Ethernet USB IC/X1+
- net Net-(T1-X1-) renamed /05 Ethernet USB IC/X1-
- net Net-(T1-X2+) renamed /05 Ethernet USB IC/X2+
- net Net-(T1-X2-) renamed /05 Ethernet USB IC/X2-
- net Net-(T1-X3+) renamed /05 Ethernet USB IC/X3+
- net Net-(T1-X3-) renamed /05 Ethernet USB IC/X3-
- net Net-(T1-X4+) renamed /05 Ethernet USB IC/X4+
- net Net-(T1-X4-) renamed /05 Ethernet USB IC/X4-
- U11 pad 44: HUB1_DS2_RXN -> HUB1_DS2_RXP
- U11 pad 45: HUB1_DS2_RXP -> HUB1_DS2_RXN
- U11 pad 50: HUB1_DS1_RXN -> HUB1_DS1_RXP
- U11 pad 51: HUB1_DS1_RXP -> HUB1_DS1_RXN
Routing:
- net HUB1_DS3_RXN: track 0.00 -> 26.0 mm
- net HUB1_DS3_RXP: track 0.00 -> 25.6 mm
- net HUB1_DS2_RXP: track 0.00 -> 25.4 mm
- net HUB1_DS2_RXN: track 0.00 -> 25.4 mm
- net HUB1_DS1_RXP: track 0.00 -> 22.6 mm
- net HUB1_DS1_RXN: track 0.00 -> 22.6 mm
- net /04 Hub Controller/HUB1_DS2_1_TXN: track 0.00 -> 20.3 mm
- net /04 Hub Controller/HUB1_DS2_1_TXP: track 0.00 -> 20.3 mm
- net /04 Hub Controller/HUB1_DS1_1_TXP: track 0.00 -> 18.4 mm
- net /04 Hub Controller/HUB1_DS1_1_TXN: track 0.00 -> 18.4 mm
- net /04 Hub Controller/HUB1_DS3_1_TXN: track 0.00 -> 16.9 mm, vias 0 -> 2
- net /04 Hub Controller/HUB1_DS3_1_TXP: track 0.00 -> 16.4 mm, vias 0 -> 2
- net GND: track 85.4 -> 80.0 mm, vias 87 -> 86
- net /02 USB UFP/UFP_RX-: track 5.16 -> 0.00 mm
- net /02 USB UFP/UFP_RX+: track 5.16 -> 0.00 mm
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- added copper zone on B.Cu, net +1V2
- added copper zone on B.Cu, net GND
- added copper zone on B.Cu, net Net-(D3-K)
- removed copper zone on F.Cu, net +1V2
- removed copper zone on F.Cu, net Net-(D3-K)
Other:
- board size 214.6 x 214.6 mm -> 92 x 92 mm
- copper layers 4 -> 6

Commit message: working on pcb
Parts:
- C26, C27, C28, C29, C35, C36, C37, C38, C40, C41, C42: moved to F.Cu
- D11, D13, D9: moved to B.Cu
- moved H1 125.6 mm to (152.8, 157.3)
- moved H3 108.5 mm to (112.5, 175.1)
- moved H4 69.7 mm to (79.1, 150.4)
- moved H2 58.2 mm to (122.9, 97.4)
- moved R39 24.0 mm to (157.1, 138.1), turned to 0 degrees
- moved C118 23.5 mm to (154.6, 139.1), turned to 0 degrees
- moved D11 22.1 mm to (145.3, 158.6), turned to 180 degrees
- moved C121 21.5 mm to (154.6, 140.6), turned to 0 degrees
- moved U13 20.2 mm to (157.8, 140.7), turned to 90 degrees
- moved C120 19.5 mm to (154.6, 142.1), turned to 0 degrees
- moved C115 16.7 mm to (156.2, 130.6), turned to 180 degrees
- moved C114 16.5 mm to (153.9, 123.0)
- moved C116 16.5 mm to (153.9, 124.5)
- moved C117 16.5 mm to (153.9, 126.0)
- moved R38 16.5 mm to (156.4, 122.1)
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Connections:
- U11 pad 14: HUB1_DS4_RXN -> HUB1_DS4_RXP
- U11 pad 15: HUB1_DS4_RXP -> HUB1_DS4_RXN
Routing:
- net HUB1_DS4_DP: track 0.00 -> 76.6 mm
- net HUB1_DS4_DN: track 0.00 -> 75.6 mm
- net HUB1_DS4_RXP: track 0.00 -> 32.1 mm
- net HUB1_DS4_RXN: track 0.00 -> 31.6 mm
- net /04 Hub Controller/HUB1_DS4_1_TXP: track 0.00 -> 31.4 mm
- net /04 Hub Controller/HUB1_DS4_1_TXN: track 0.00 -> 30.9 mm
- net USB_UFP_CC2: track 0.00 -> 29.7 mm, vias 0 -> 4
- net HUB1_DS2_RXP: track 25.4 -> 0.77 mm
- net HUB1_DS2_RXN: track 25.4 -> 0.77 mm
- net HUB1_DS1_RXP: track 22.6 -> 0.00 mm
- net HUB1_DS1_RXN: track 22.6 -> 0.00 mm
- net HUB1_DS3_RXN: track 26.0 -> 5.46 mm
- net /04 Hub Controller/HUB1_DS2_1_TXN: track 20.3 -> 0.00 mm
- net /04 Hub Controller/HUB1_DS2_1_TXP: track 20.3 -> 0.00 mm
- net HUB1_DS3_RXP: track 25.6 -> 5.46 mm
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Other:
- board size 92 x 92 mm -> 89.8 x 89.8 mm
